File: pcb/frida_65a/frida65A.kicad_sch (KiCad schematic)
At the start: 44 parts, among them J1 CONN_PWR, J10 TP_LOGIC, J11 TP_OUT, J2 CONN_IN_P, J3 CONN_IN_N, J4 TP_CFG, J5 CONN_CFG, J6 TP_IN, J7 TP_INIT, J8 TP_SAMP, J9 TP_COMP, U1 DUT

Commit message: Update pcb
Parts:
- removed J1: CONN_PWR, Silab:Molex_Mini-Fit_Jr_02x04_horizontal, symbol silab:Molex_02x04_Mini-Fit_Jr
- removed JP1: Analog, symbol Jumper:Jumper_3_Open
- removed JP2: Digital, symbol Jumper:Jumper_3_Open
- removed JP3: DAC, symbol Jumper:Jumper_3_Open
- removed JP4: IO, symbol Jumper:Jumper_3_Open
- added C18: 47u, Capacitor_SMD:C_0603_1608Metric, symbol Device:C
- added C19: 1u, Capacitor_SMD:C_0603_1608Metric, symbol Device:C
- added C20, C21: 100n, Capacitor_SMD:C_0603_1608Metric, symbol Device:C
- added FB1, FB2, FB3, FB4, FB5: FerriteBead_Small, Resistor_SMD:R_0603_1608Metric, symbol Device:FerriteBead_Small
- added J1: TP_PWR, Silab:Molex_Mini-Fit_Jr_02x04_horizontal, symbol Connector:Conn_01x06_Pin
- added J12: J_P, symbol Connector_Generic:Conn_02x02_Top_Bottom
- added J13, J14, J15: 469914004, CONN_SD-46991-001_04_MOL, symbol frida:469914004
- added J16: J_N, symbol Connector_Generic:Conn_02x02_Top_Bottom
- added R10, R11, R12, R6, R7, R8, R9: 10k, Resistor_SMD:R_0603_1608Metric, symbol Device:R
- added TH1: Thermistor_NTC, symbol Device:Thermistor_NTC
- added U2: THS4520RGTT, frida65A:QFN50P300X300X100-17N, symbol frida:THS4520RGTT
- C1, C10, C11, C12, C13, C14, C15, C16, C2, C3, C4, C5, C6, C7, C8, C9: footprint Capacitor_SMD:C_0201_0603Metric -> Capacitor_SMD:C_0603_1608Metric
- C17: footprint (none) -> Capacitor_SMD:C_0603_1608Metric
- DP1: footprint Silab:DP_Molex_47272-0024 -> silab:DP_Molex_47272-0024
- R1, R2, R3, R4: footprint (none) -> Resistor_SMD:R_0603_1608Metric
- R13: renamed from R6; footprint (none) -> Resistor_SMD:R_0603_1608Metric
- R5: value 100 -> 10k; footprint (none) -> Resistor_SMD:R_0603_1608Metric
- U1: footprint (none) -> frida65A:frida
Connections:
- net CLK_COMP_N: now also DP1.4, R2.1, R10.1; no longer DP1.7, R3.1
- net CLK_COMP_P: now also DP1.6, R2.2, R9.1; no longer DP1.9, R3.2
- net CLK_INIT_N: now also DP1.10, R4.1, R6.1; no longer DP1.1, R1.1
- net CLK_INIT_P: now also DP1.12, R4.2, R5.1; no longer DP1.3, R1.2
- net CLK_LOGIC_N: now also DP1.1, R1.1, R12.1; no longer DP1.10, R4.1
- net CLK_LOGIC_P: now also DP1.3, R1.2, R11.1; no longer DP1.12, R4.2
- net CLK_SAMP_N: now also DP1.7, R3.1, R8.1; no longer DP1.4, R2.1
- net CLK_SAMP_P: now also DP1.9, R3.2, R7.1; no longer DP1.6, R2.2
- net COMP_OUT_N: now also DP1.17, J11.1 (Pin_1); no longer DP1.15, J11.2 (Pin_2), R5.1
- net COMP_OUT_P: now also DP1.15, J11.2 (Pin_2); no longer DP1.17, J11.1 (Pin_1), R5.2
- net GND: now also R5.2, C18.2, C19.2, C20.2, C21.2, J1.6 (Pin_6), J13.3, J13.4, J14.3, J14.4, J15.3, J15.4, R10.2, R11.2, R12.2, R6.2, R7.2, R8.2, R9.2, U2.13 (VS-), U2.14 (VS-__1), U2.15 (VS-__2), U2.16 (VS-__3), U2.17 (EP)
- net VDD_A: now also FB2.2, J1.2 (Pin_2)
- net VDD_D: now also FB1.2, J1.1 (Pin_1)
- net VDD_DAC: now also FB3.2, J1.3 (Pin_3)
- net VDD_IO: now also DP1.19, FB4.2, J1.4 (Pin_4)
- net at J6.2 (Pin_2), U1.24 (VIN_N): now also J16.3 (Pin_3), J16.4 (Pin_4); no longer J3.1 (In)
- net at J6.1 (Pin_1), U1.25 (VIN_P): now also J12.3 (Pin_3), J12.4 (Pin_4); no longer J2.1 (In)
- net at DP1.13: now also TH1.1
- net at DP1.14: now also TH1.2
- new net: J16.1 (Pin_1), U2.10 (VOUT-)
- new net: J12.1 (Pin_1), U2.3 (VOUT+)
- new net: FB1.1, J13.1
- new net: FB2.1, J13.2
- new net: FB4.1, J14.2
- new net: FB5.1, J15.1, J15.2
- new net: FB3.1, J14.1
- new net VDD_DIF: C18.1, C19.1, C20.1, C21.1, FB5.2, J1.5 (Pin_5), U2.5 (VS+), U2.6 (VS+__1), U2.7 (VS+__2), U2.8 (VS+__3)
- new net VIN_N_EXT: J16.2 (Pin_2), J3.1 (In)
- new net VIN_P_EXT: J2.1 (In)
- no-connect marks 3 -> 5
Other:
- note added: "Note the L0 - L3 diff pair positions invert in cable"
- note added: "Place pull downs further from DUT, and diff resistors closer"
- note removed: "pull-ups/downs & filtering?"
- note removed: "this inversion necessary? is the Zout here right?"
- moved on the sheet: C1, C10, C11, C12, C13, C14, C15, C16, C17, C2, C3, C4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

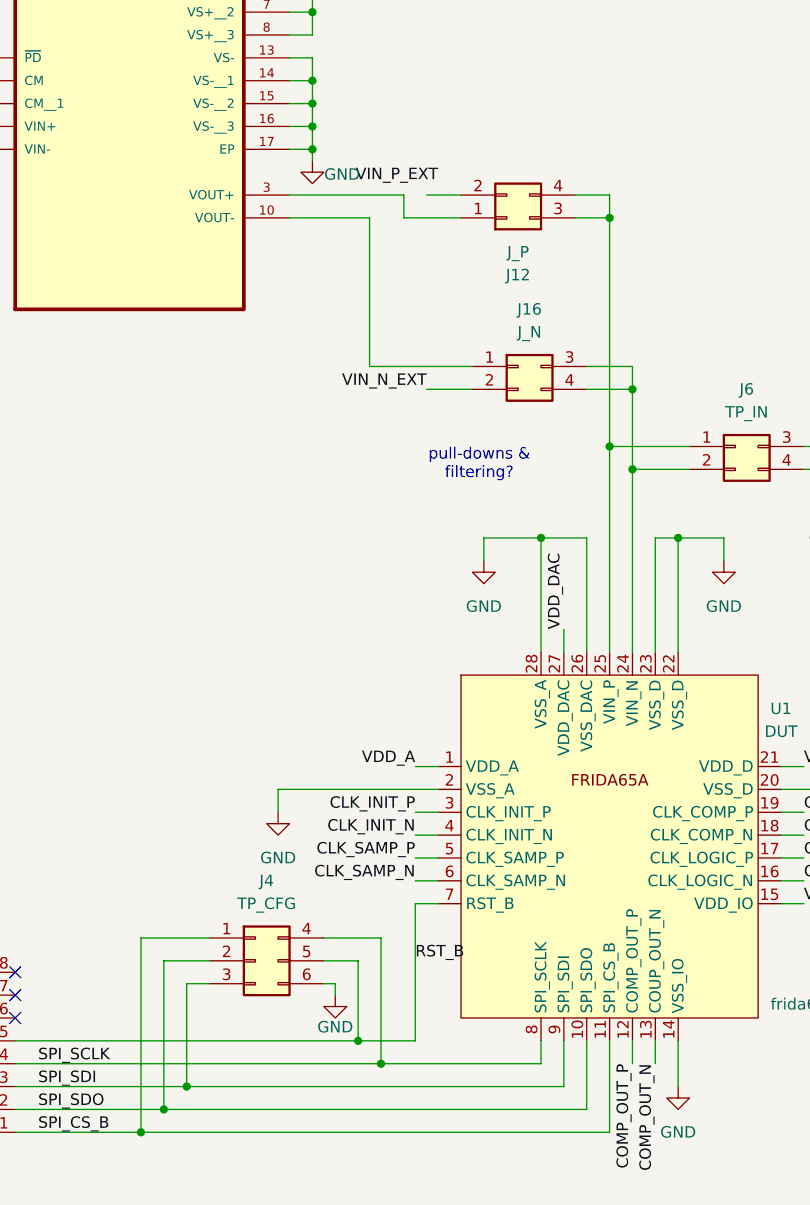
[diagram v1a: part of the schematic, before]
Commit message: Replace PostEvaluator with direct pickle loading so our expression functions actually work
- Load .pck files directly and inject flow.expression as 'm' into eval environment
- Auto-detect local vs remote for make sim (no more host= parameter)
- Add checks for spectre/lmstat in PATH before trying to simulate
- Suppress matplotlib font manager spam in logs
- PCB and OpenROAD stage updates
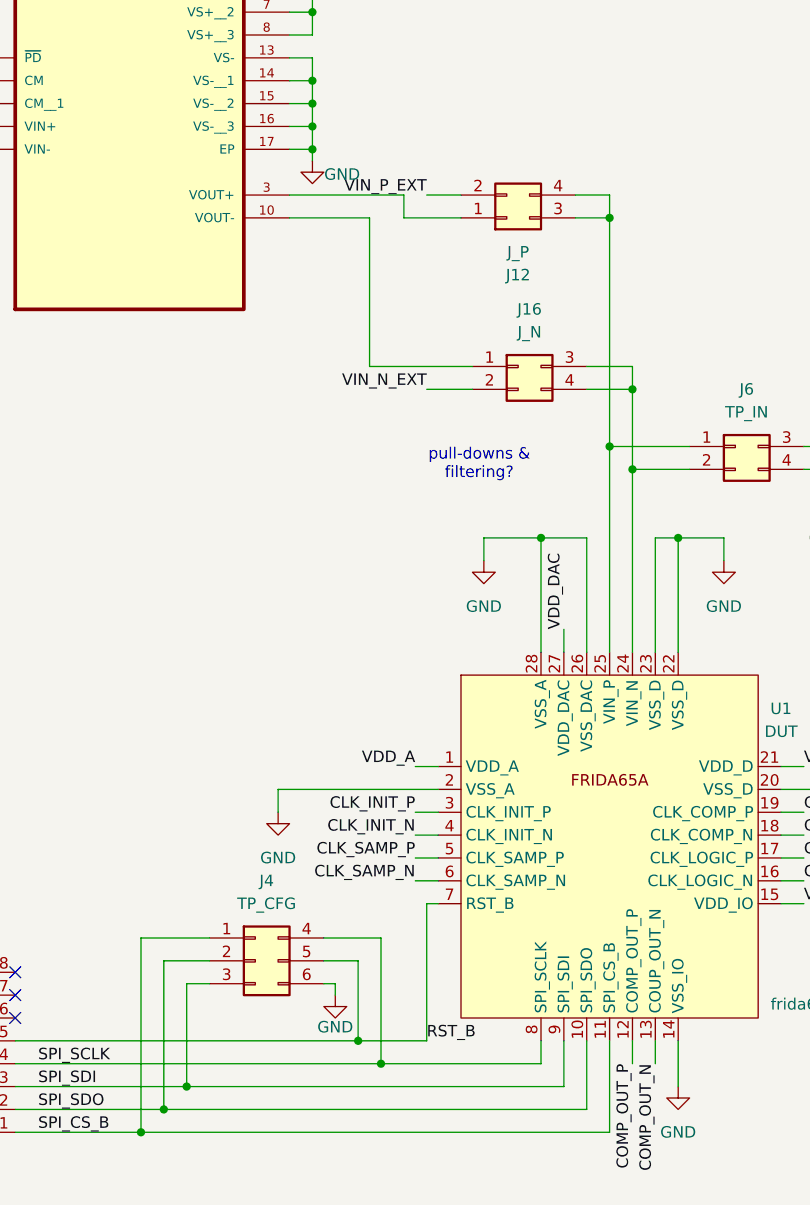
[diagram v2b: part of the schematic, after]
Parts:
- DP1: footprint silab:DP_Molex_47272-0024 -> frida65A:displayport
- H1, H2, H3, H4: footprint (none) -> MountingHole:MountingHole_3.2mm_M3_Pad_Via
- J1: footprint Silab:Molex_Mini-Fit_Jr_02x04_horizontal -> frida65A:Molex_Mini-Fit_Jr_5569-08A1_2x04_P4.20mm_Horizontal
- J12: footprint (none) -> frida65A:Molex_Mini-Fit_Jr_5569-08A1_2x04_P4.20mm_Horizontal
- J13, J14, J15: footprint CONN_SD-46991-001_04_MOL -> frida65A:CONN_SD-46991-001_04_MOL
- J16: footprint (none) -> frida65A:displayport
- J3: footprint import:TE_3-1478978-1 -> Connector_Coaxial:SMA_Amphenol_901-143_Horizontal
- TH1: footprint (none) -> Resistor_SMD:R_0603_1608Metric
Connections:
- net VIN_P_EXT: now also J12.2 (Pin_2)
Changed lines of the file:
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@@
 	(wire
 		(pts
-			(xy 219.71 148.59) (xy 226.06 148.59)
+			(xy 219.71 148.59) (xy 227.33 148.59)
 		)
 		(stroke
@@
 	(wire
 		(pts
+			(xy 227.33 133.35) (xy 227.33 148.59)
+		)
+		(stroke
+			(width 0)
+			(type default)
+		)
+	)
+	(wire
+		(pts
 			(xy 90.17 138.43) (xy 90.17 139.7)
 		)
@@
 	(wire
 		(pts
-			(xy 226.06 133.35) (xy 228.6 133.35)
+			(xy 227.33 133.35) (xy 228.6 133.35)
 		)
 		(stroke
@@
 	(wire
 		(pts
-			(xy 226.06 133.35) (xy 226.06 148.59)
-		)
-		(stroke
-			(width 0)
-			(type default)
-		)
-	)
-	(wire
-		(pts
 			(xy 43.18 25.4) (xy 48.26 25.4)
 		)
@@
 	)
 	(label "VIN_P_EXT"
-		(at 228.6 53.34 180)
+		(at 227.33 54.61 180)
 		(effects
 			(font
@@
 	)
 	(label "RST_B"
-		(at 226.06 139.7 0)
+		(at 227.33 148.59 0)
 		(effects
 			(font
@@
 			)
 		)
-		(property "Footprint" ""
+		(property "Footprint" "MountingHole:MountingHole_3.2mm_M3_Pad_Via"
 			(at 34.29 165.1 0)
 			(effects
@@
 			)
 		)
-		(property "Footprint" "CONN_SD-46991-001_04_MOL"
+		(property "Footprint" "frida65A:CONN_SD-46991-001_04_MOL"
 			(at 19.304 102.616 0)
 			(effects
@@
 			)
 		)
-		(property "Footprint" "Silab:Molex_Mini-Fit_Jr_02x04_horizontal"
+		(property "Footprint" "frida65A:Molex_Mini-Fit_Jr_5569-08A1_2x04_P4.20mm_Horizontal"
 			(at 76.2 133.35 0)
 			(effects
@@
 			)
 		)
-		(property "Footprint" "import:TE_3-1478978-1"
+		(property "Footprint" "Connector_Coaxial:SMA_Amphenol_901-143_Horizontal"
 			(at 154.94 54.61 0)
 			(effects
@@
 			)
 		)
-		(property "Footprint" ""
+		(property "Footprint" "Resistor_SMD:R_0603_1608Metric"
 			(at 52.07 72.39 0)
 			(effects
@@
 			)
 		)
-		(property "Footprint" "CONN_SD-46991-001_04_MOL"
+		(property "Footprint" "frida65A:CONN_SD-46991-001_04_MOL"
 			(at 19.304 133.096 0)
 			(effects
@@
 			)
 		)
-		(property "Footprint" "silab:DP_Molex_47272-0024"
+		(property "Footprint" "frida65A:displayport"
 			(at 16.51 105.156 0)
 			(effects
@@
 			)
 		)
-		(property "Footprint" ""
+		(property "Footprint" "MountingHole:MountingHole_3.2mm_M3_Pad_Via"
 			(at 24.13 182.88 0)
 			(effects
@@
 			)
 		)
-		(property "Footprint" ""
+		(property "Footprint" "frida65A:Molex_Mini-Fit_Jr_5569-08A1_2x04_P4.20mm_Horizontal"
 			(at 236.22 57.15 0)
 			(effects
@@
 			)
 		)
-		(property "Footprint" "CONN_SD-46991-001_04_MOL"
+		(property "Footprint" "frida65A:CONN_SD-46991-001_04_MOL"
 			(at 19.304 117.856 0)
 			(effects
@@
 			)
 		)
-		(property "Footprint" ""
+		(property "Footprint" "MountingHole:MountingHole_3.2mm_M3_Pad_Via"
 			(at 24.13 165.1 0)
 			(effects
@@
 			)
 		)
-		(property "Footprint" ""
+		(property "Footprint" "MountingHole:MountingHole_3.2mm_M3_Pad_Via"
 			(at 34.29 182.88 0)
 			(effects
@@
 			)
 		)
-		(property "Footprint" ""
+		(property "Footprint" "frida65A:displayport"
 			(at 237.49 73.66 0)
 			(effects

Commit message: Finishing design review slides
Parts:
- added C22: 100n, Capacitor_SMD:C_0603_1608Metric, symbol Device:C
- added R14, R15: 499, Resistor_SMD:R_0603_1608Metric, symbol Device:R
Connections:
- net GND: now also C22.1
- net at J16.1 (Pin_1), U2.10 (VOUT-): now also R15.2
- net AMP_EN: now reaches U2.12 (~{PD})
- net AMP_EN: now also J5.6
- net at J12.1 (Pin_1), U2.3 (VOUT+): now also R14.2
- no-connect marks 5 -> 4
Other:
- moved on the sheet: DP1, H1, H2, J2, J3
